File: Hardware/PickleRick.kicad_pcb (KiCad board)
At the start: 4 copper layers, 100 x 37 mm, 218 parts, among them IC1 TPS259830ONRGER, J1 RBUS, J10 Conn_Coaxial, J11 Conn_Coaxial, J12 Conn_01x03_Male, J13 Conn_01x03_Pin, J14 Conn_01x07_Socket, J2 Conn_01x02_Male, J3 ST1W008S4TR2000, J4 Conn_01x03_Pin, J5 USB_C_Receptacle_USB2.0, J6 Screw_Terminal_01x08, J7 Conn_01x05_Male, J8 DeployLipo, J9 UCLipo, Q1 PMV20ENR, Q10 DMP3099L, Q11 SQS141ELNW-T1_GE3, Q12 SQS141ELNW-T1_GE3, Q2 BUK9M11-40EX, Q3 BUK9M11-40EX, Q4 BUK9M11-40EX, Q5 BUK9M11-40EX, Q8 DMP3099L, Q9 DMP3099L, U1 ESP32-S3, U10 LTC4412xS6, U11 MP28167GQ-A-Z, U14 LTC4412xS6, U16 SC4215, U17 LTC4412xS6, U19 MAX-M10S, U2 DPS368, U20 SN65HVD230, U21 RFM95W-868S2, U22 LTC4412xS6, U3 LTV-247, U4 PCA9534RGVR, U5 PCA9685BS, U6 H3LIS331DLTR, U7 ICM-20608-G, U8 MMC5983MA, U9 LTC4412xS6, Y1 R940000171

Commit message: hardware complete
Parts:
- added G**: orientation_marker, iclr-hw:orientation_marker, F.Cu at (143.4, 83.0)
- moved TP24 12.0 mm to (120.2, 79.1)
- moved G*** 1.72 mm to (131.4, 74.2)
- moved G*** 1.13 mm to (125.2, 74.2)
- moved R8 0.82 mm to (120.8, 77.6), turned to 0 degrees
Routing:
- net /PPS: track 12.9 -> 7.84 mm
- net /JTAG_MTCK: track 84.8 -> 85.9 mm
- net /CHIP_PU: track 34.5 -> 35.5 mm
- net /BOOT: track 25.9 -> 27.0 mm
- net /SDA: track 144.0 -> 143.3 mm
- net /HSPI_MISO: track 74.7 -> 74.1 mm
- net /nukes/Cont3: track 5.51 -> 4.99 mm
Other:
- board text added: "+"
- board text added: "EXT"
- board text added: "NUKES +-"
- board text removed: "EXP"
- board text removed: "NUKES"

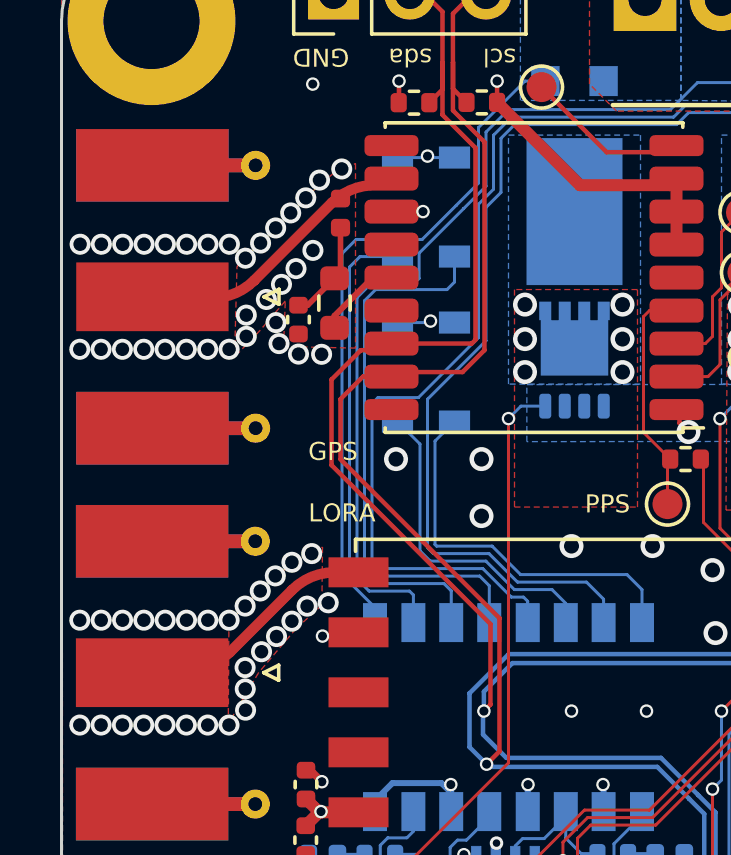
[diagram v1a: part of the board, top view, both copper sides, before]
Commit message: updated antenna trace widths
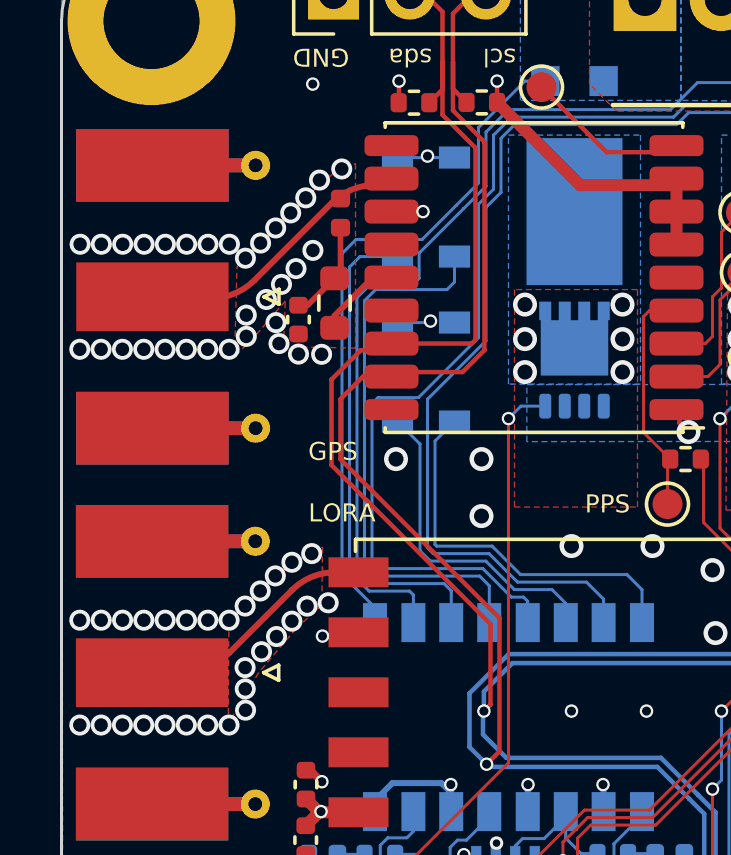
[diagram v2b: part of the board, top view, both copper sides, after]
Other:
- copper layers 4 -> 6
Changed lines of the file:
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@@
 		(1 "In1.Cu" power)
 		(2 "In2.Cu" power)
+		(3 "In3.Cu" signal)
+		(4 "In4.Cu" signal)
 		(31 "B.Cu" signal)
 		(32 "B.Adhes" user "B.Adhesive")
@@
 			(layer "dielectric 2"
 				(type "core")
-				(thickness 1.275)
+				(thickness 0.5525)
 				(material "FR4")
 				(epsilon_r 4.5)
@@
 				(loss_tangent 0.02)
 			)
+			(layer "In3.Cu"
+				(type "copper")
+				(thickness 0.035)
+			)
+			(layer "dielectric 4"
+				(type "core")
+				(thickness 0.5525)
+				(material "FR4")
+				(epsilon_r 4.5)
+				(loss_tangent 0.02)
+			)
+			(layer "In4.Cu"
+				(type "copper")
+				(thickness 0.035)
+			)
+			(layer "dielectric 5"
+				(type "prepreg")
+				(thickness 0.1)
+				(material "FR4")
+				(epsilon_r 4.5)
+				(loss_tangent 0.02)
+			)
 			(layer "B.Cu"
 				(type "copper")
@@
 		(start 109.014213 69.055787)
 		(end 106.425786 71.644214)
-		(width 0.349402)
+		(width 0.2)
 		(layer "F.Cu")
 		(net 81)
@@
 		(mid 105.836987 72.051728)
 		(end 105.142542 72.228203)
-		(width 0.349402)
+		(width 0.2)
 		(layer "F.Cu")
 		(net 81)
@@
 		(mid 109.603014 68.648281)
 		(end 109.014213 69.055787)
-		(width 0.349402)
+		(width 0.2)
 		(layer "F.Cu")
 		(net 81)
@@
 		(start 105.615787 84.034213)
 		(end 107.689214 81.960786)
-		(width 0.349402)
+		(width 0.2)
 		(layer "F.Cu")
 		(net 82)
@@
 		(mid 105.026987 84.441727)
 		(end 105.615787 84.034213)
-		(width 0.349402)
+		(width 0.2)
 		(layer "F.Cu")
 		(net 82)
@@
 		(mid 108.33806 81.527241)
 		(end 109.103427 81.375)
-		(width 0.349402)
+		(width 0.2)
 		(layer "F.Cu")
 		(net 82)

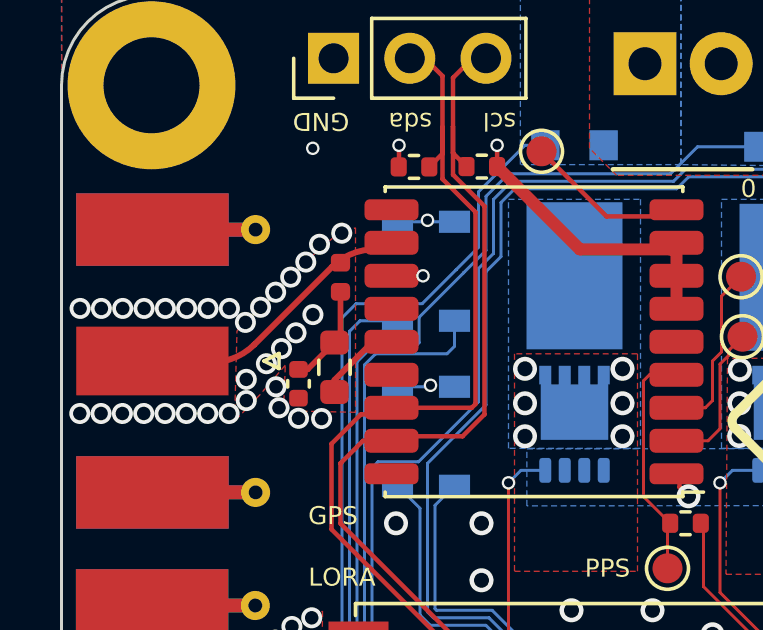
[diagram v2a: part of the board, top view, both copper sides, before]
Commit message: added planes
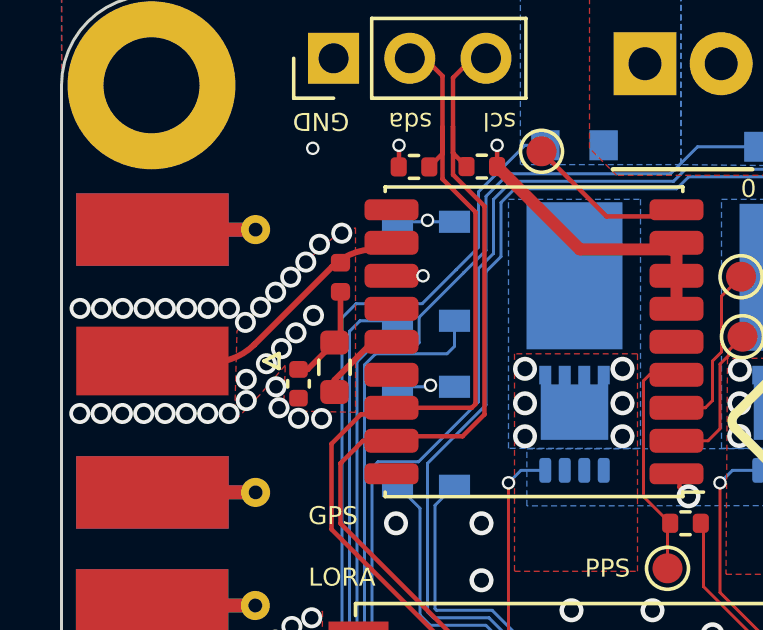
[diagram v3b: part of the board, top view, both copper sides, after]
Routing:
- added copper zone on In4.Cu, net +3V3
- added copper zone on In3.Cu, net GND
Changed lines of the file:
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@@
 	)
 	(via
-		(at 108.380614 70.643558)
+		(at 108.4 70.67)
 		(size 0.7)
 		(drill 0.45)
@@
 		(net_name "GND")
 		(layer "In1.Cu")
-		(hatch edge 0.508)
+		(hatch edge 0.5)
+		(priority 1)
 		(connect_pads yes
 			(clearance 0.254)
 		)
-		(min_thickness 0.254)
+		(min_thickness 0.25)
 		(filled_areas_thickness no)
 		(fill yes
-			(thermal_gap 0.3)
-			(thermal_bridge_width 1.5)
+			(thermal_gap 0.5)
+			(thermal_bridge_width 0.5)
 		)
 		(polygon
 			(pts
-				(xy 200 97) (xy 100 97) (xy 100 60) (xy 200 60)
+				(xy 151.7 60.6) (xy 159.7 60.6) (xy 159.7 64.9) (xy 151.7 64.9)
 			)
 		)
@@
 		(polygon
 			(pts
-				(xy 151.7 60.6) (xy 159.7 60.6) (xy 159.7 64.9) (xy 151.7 64.9)
+				(xy 140.4 60.7) (xy 144.1 60.7) (xy 144.1 64) (xy 140.4 64)
 			)
 		)
@@
 		(net 2)
 		(net_name "GND")
-		(layer "In1.Cu")
-		(hatch edge 0.5)
-		(priority 1)
+		(layers "In1.Cu" "In3.Cu")
+		(hatch edge 0.508)
 		(connect_pads yes
 			(clearance 0.254)
 		)
-		(min_thickness 0.25)
+		(min_thickness 0.254)
 		(filled_areas_thickness no)
 		(fill yes
-			(thermal_gap 0.5)
-			(thermal_bridge_width 0.5)
+			(thermal_gap 0.3)
+			(thermal_bridge_width 1.5)
 		)
 		(polygon
 			(pts
-				(xy 140.4 60.7) (xy 144.1 60.7) (xy 144.1 64) (xy 140.4 64)
+				(xy 200 97) (xy 100 97) (xy 100 60) (xy 200 60)
 			)
 		)
@@
 		(net 1)
 		(net_name "+3V3")
-		(layer "In2.Cu")
+		(layers "In2.Cu" "In4.Cu")
 		(hatch edge 0.508)
 		(connect_pads yes
